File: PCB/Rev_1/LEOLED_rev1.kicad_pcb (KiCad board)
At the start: 2 copper layers, 84.1 x 40 mm, 96 parts, among them J1 PHEONIX_MPT_1725698, J2 USB_MicroB, J3 PHOENIX_MPT_1725656, J4 WURTH_61300411121, J5 FTSH-105-01-F-DV-K, J7 PHOENIX_MPT_1725656, M1 MountigHole_M2, M2 MountigHole_M2, M3 MountigHole_M2, M4 MountigHole_M2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

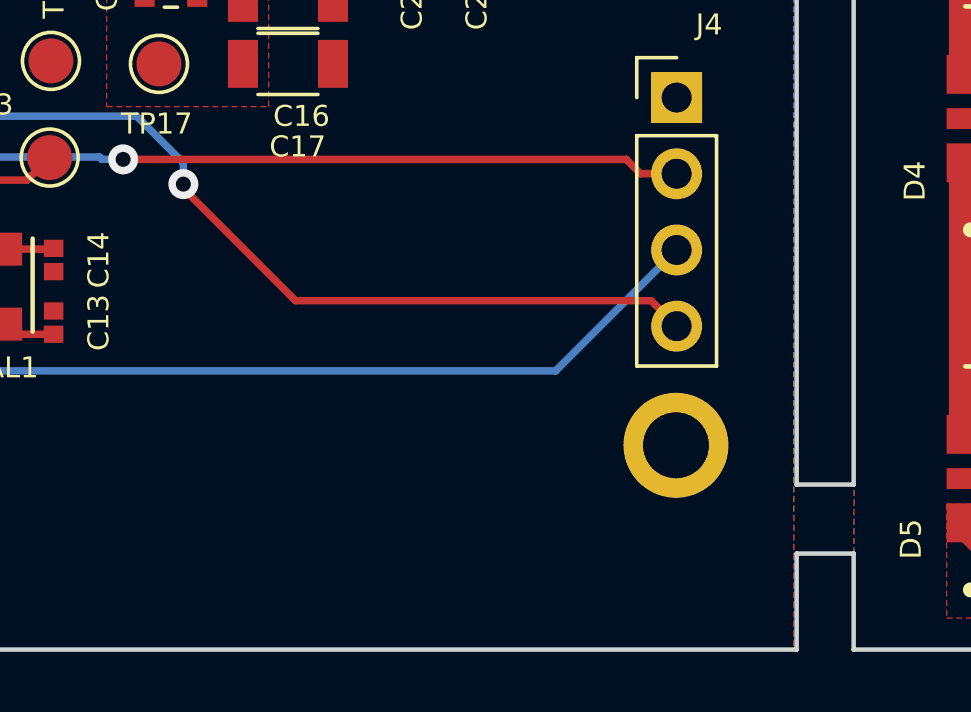
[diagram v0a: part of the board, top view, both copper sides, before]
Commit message: UART header not fitted
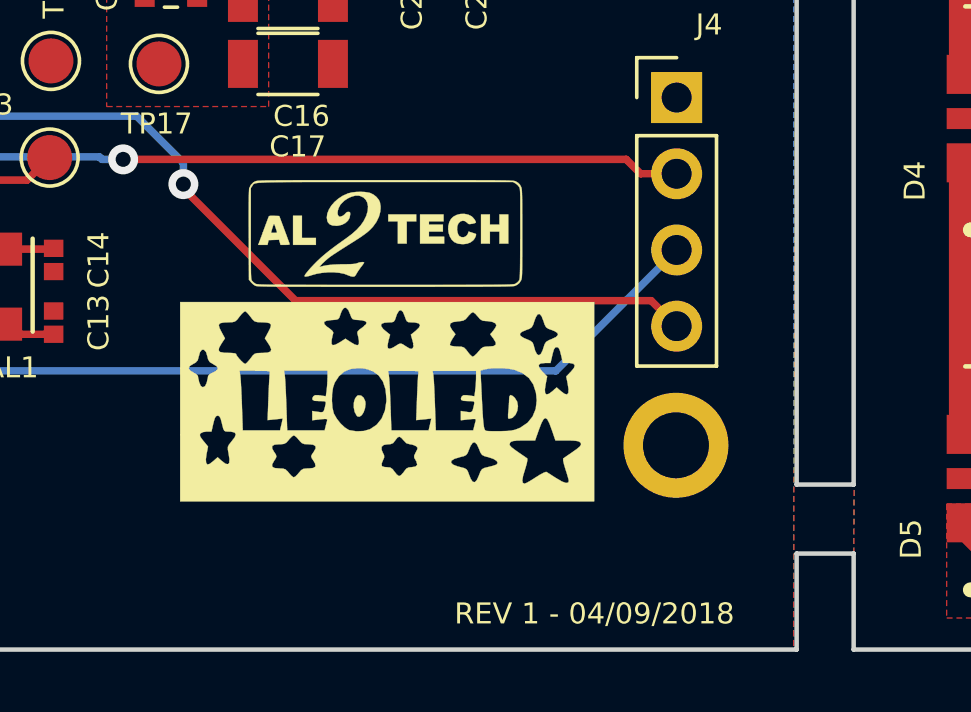
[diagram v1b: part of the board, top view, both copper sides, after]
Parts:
- added G***: LOGO, AL2TECH:AL2TECH_logo, F.Cu at (198.4, 124.1)
- added G***: LOGO, AL2TECH:LEOLED_logo, F.Cu at (198.5, 129.7)
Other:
- board text added: "REV 1 - 04/09/2018"

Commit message: Adding gerber job file and PDFs
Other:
- board text added: "+"
- board text added: "-"
- board text added: "BAT GND NTCN NTCP GND SOL"
- board text added: "G"
- board text added: "RX"
- board text added: "TX"
- board text added: "VDD"
